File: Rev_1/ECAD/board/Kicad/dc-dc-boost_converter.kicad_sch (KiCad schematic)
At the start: 56 parts, among them Q1 IPP029N15NM6, Q2 NPN, U1 LM3478MA, U2 LM358, U3 LM358

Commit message: Components for 15V regulator are placed
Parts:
- removed C12: 1u, Capacitor_SMD:C_0805_2012Metric_Pad1.18x1.45mm_HandSolder, symbol Device:C_Small
- removed Q?: PMOS, symbol Simulation_SPICE:PMOS
- removed R? (x2): ?, symbol Device:R
- removed R?: 20m, symbol Device:R
- removed R? (x3): 10k, symbol Device:R
- added C1, C115: 100n, Capacitor_SMD:C_0603_1608Metric_Pad1.08x0.95mm_HandSolder, symbol Device:C
- added C116: 10p, Capacitor_SMD:C_0603_1608Metric_Pad1.08x0.95mm_HandSolder, symbol Device:C
- added C117, C124, C3, C4: 100n, Capacitor_SMD:C_0603_1608Metric_Pad1.08x0.95mm_HandSolder, symbol Device:C_Small
- added C118: 100u, Capacitor_SMD:CP_Elec_10x10.5, symbol Device:C_Small
- added C119: 1u, Capacitor_SMD:C_0603_1608Metric_Pad1.08x0.95mm_HandSolder, symbol Device:C_Small
- added C120: 10u, Capacitor_SMD:C_0805_2012Metric_Pad1.18x1.45mm_HandSolder, symbol Device:C_Small
- added C121: 220u, Capacitor_SMD:CP_Elec_10x10.5, symbol Device:C_Small
- added C123: 1u, Capacitor_SMD:C_0805_2012Metric_Pad1.18x1.45mm_HandSolder, symbol Device:C_Small
- added D100: D_TVS, Diode_SMD:D_0805_2012Metric_Pad1.15x1.40mm_HandSolder, symbol Device:D_TVS
- added FB100: 100, Inductor_SMD:L_0805_2012Metric_Pad1.15x1.40mm_HandSolder, symbol Device:FerriteBead_Small
- added Q101, Q2: NPN, Package_TO_SOT_SMD:SOT-23_Handsoldering, symbol Simulation_SPICE:NPN
- added Q103: PMOS, Package_TO_SOT_SMD:TO-252-2, symbol Simulation_SPICE:PMOS
- added R1, R107, R110, R14, R15, R3, R9: 10k, Resistor_SMD:R_0805_2012Metric_Pad1.20x1.40mm_HandSolder, symbol Device:R
- added R10, R11, R13, R4, R5, R8: 1k, Resistor_SMD:R_0805_2012Metric_Pad1.20x1.40mm_HandSolder, symbol Device:R
- added R109: 20m, Resistor_SMD:R_1206_3216Metric_Pad1.30x1.75mm_HandSolder, symbol Device:R
- added R111: 100k, Resistor_SMD:R_0805_2012Metric_Pad1.20x1.40mm_HandSolder, symbol Device:R
- added R112, R115, R116: 100, Resistor_SMD:R_0805_2012Metric_Pad1.20x1.40mm_HandSolder, symbol Device:R
- added R113, R114: ?, Resistor_SMD:R_0603_1608Metric_Pad0.98x0.95mm_HandSolder, symbol Device:R
- added R2: 4k7, Resistor_SMD:R_0805_2012Metric_Pad1.20x1.40mm_HandSolder, symbol Device:R
- added RV100: 10k, filip:Potentiometer_SMD_Trimmer_PVG3_3.6x3, symbol Device:R_Potentiometer_Trim
- added SW1: SW_DIP_x04, symbol Switch:SW_DIP_x04
- added unit 3 of U2
- added unit 3 of U3
- C103: renamed from C4; footprint Capacitor_SMD:C_0805_2012Metric_Pad1.18x1.45mm_HandSolder -> Capacitor_SMD:C_0603_1608Metric_Pad1.08x0.95mm_HandSolder
- C104: renamed from C5; footprint Capacitor_SMD:C_0805_2012Metric_Pad1.18x1.45mm_HandSolder -> Capacitor_SMD:C_0603_1608Metric_Pad1.08x0.95mm_HandSolder
- C105: renamed from C6; footprint Capacitor_SMD:C_0805_2012Metric_Pad1.18x1.45mm_HandSolder -> Capacitor_SMD:C_0603_1608Metric_Pad1.08x0.95mm_HandSolder
- C106: renamed from C7; footprint Capacitor_SMD:C_0805_2012Metric_Pad1.18x1.45mm_HandSolder -> Capacitor_SMD:C_0603_1608Metric_Pad1.08x0.95mm_HandSolder
- C107: renamed from C8; footprint Capacitor_SMD:C_0805_2012Metric_Pad1.18x1.45mm_HandSolder -> Capacitor_SMD:C_0603_1608Metric_Pad1.08x0.95mm_HandSolder
- C108: renamed from C9; footprint Capacitor_SMD:C_0805_2012Metric_Pad1.18x1.45mm_HandSolder -> Capacitor_SMD:C_0603_1608Metric_Pad1.08x0.95mm_HandSolder
- C109: renamed from C10; footprint Capacitor_SMD:C_0805_2012Metric_Pad1.18x1.45mm_HandSolder -> Capacitor_SMD:C_0603_1608Metric_Pad1.08x0.95mm_HandSolder
- C111: renamed from C11; footprint Capacitor_SMD:C_0805_2012Metric_Pad1.18x1.45mm_HandSolder -> Capacitor_SMD:C_0603_1608Metric_Pad1.08x0.95mm_HandSolder
- C2: renamed from C?; footprint (none) -> Capacitor_SMD:C_0603_1608Metric_Pad1.08x0.95mm_HandSolder
- D1, D2: renamed from D?; footprint (none) -> LED_SMD:LED_0805_2012Metric_Pad1.15x1.40mm_HandSolder
- L100: renamed from L1; footprint filip:IHLP5050FD -> filip:L_IHLP5050FD_5.0x5.0mm_Shielded
- Q1: renamed from Q?; footprint (none) -> Package_TO_SOT_SMD:SOT-23_Handsoldering; Mouser NO: (none) -> 637-BC817-16
- Q100: renamed from Q1; footprint filip:PSMN4R0 -> filip:TO-263-5_TabPin1-HandSoldered
- Q102: renamed from Q2; footprint (none) -> Package_TO_SOT_SMD:SOT-223-3_TabPin2; Mouser NO: (none) -> 621-ZXTN19100CGTA
- R100: renamed from R1; footprint Resistor_SMD:R_0805_2012Metric_Pad1.20x1.40mm_HandSolder -> Resistor_SMD:R_0603_1608Metric_Pad0.98x0.95mm_HandSolder
- R104: renamed from R5; footprint Resistor_SMD:R_0805_2012Metric_Pad1.20x1.40mm_HandSolder -> Resistor_SMD:R_0603_1608Metric_Pad0.98x0.95mm_HandSolder
- R106, R108, R17, R18, R19, R20, R21, R6, R7: renamed from R?; footprint (none) -> Resistor_SMD:R_0805_2012Metric_Pad1.20x1.40mm_HandSolder
- R12, R16: renamed from R?; footprint (none) -> Resistor_SMD:R_0603_1608Metric_Pad0.98x0.95mm_HandSolder
- R22, R23: renamed from R?; value 5k1 -> 4k7; footprint (none) -> Resistor_SMD:R_0805_2012Metric_Pad1.20x1.40mm_HandSolder
- R24: renamed from R?; value 10k -> 1K; footprint (none) -> Resistor_SMD:R_0805_2012Metric_Pad1.20x1.40mm_HandSolder
- gave numbers to parts that had none: 2
- renumbered C1 to C100, C2 to C101, C3 to C102, C13 to C112, C14 to C113, C15 to C114, D1 to D101, D2 to D102, R2 to R101, R3 to R102, R4 to R103, R6 to R105, U1 to U100
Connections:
- net +17V: now also Q102.2 (C), C115.2, C123.1, FB100.2, Q101.1 (C), R107.1, U2.8 (V+); no longer C111.1, C112.1, C113.1, C114.1, D101.2 (K), Q102.1 (C), R103.1
- net +5V: now also C1.2, C3.1, C4.1, R1.1, U3.8 (V+)
- net CURRENT_V_REF: now also R10.2, R11.2, R13.2, R15.2, R5.2
- net GND: now also C1.1, C115.1, C117.2, C118.2, C119.2, C120.2, C121.2, C123.2, C124.2, C3.2, C4.2, D100.1 (A1), Q2.3 (E), R111.2, R114.2, U2.4 (V-), U3.4 (V-)
- net RESET: now also C2.2
- net SHUNT_IN: now also C117.1, C118.1, R109.1
- net SHUNT_OUT: now also Q103.3 (S), R109.2, R110.1
- net SHUTDOWN: now also R112.2, R115.1
- net V_FB: now also C116.2, R113.2, R114.1
- net V_REF: now also C124.1, R107.2
- net at R108.1, U2.1: now also C116.1
- net at R108.2: now also Q101.2 (B); no longer Q102.2 (B)
- net VIN renamed V_IN
- net V_IN: now also D100.2 (A2)
- new net: Q2.2 (B), R115.2
- new net: R1.2, SW1.1, SW1.2, SW1.3, SW1.4
- new net: Q2.1 (C), R116.1
- new net: R10.1, R11.1, R4.2
- new net: R13.1, R8.2
- new net: R5.1, SW1.8
- new net: Q101.3 (E), Q102.1 (B)
- new net: R14.2, R15.1
- new net: R113.1, RV100.2
- new net: R4.1, SW1.7
- new net: R14.1, R9.2
- new net: R3.2, R9.1
- new net: R3.1, SW1.5
- new net: R2.1, SW1.6
- new net: R2.2, R8.1
- new net +15V: C119.1, C120.1, C121.1, Q103.2 (D), R116.2, RV100.1
- new net LOOP_OUT: C111.1, C112.1, C113.1, C114.1, D101.2 (K), FB100.1, R103.1
- new net MOS_G: Q103.1 (G), R110.2, R111.1, R112.1
- no-connect marks 0 -> 1
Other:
- note added: "0.5A"
- note added: "15V DC-DC"
- note added: "1A"
- note added: "2A"
- note added: "4A"
- note added: ">=100mA"
- note added: ">=5-6A"
- note added: "Bypass & Bulk Caps"
- note added: "LOW RDS_ON"
- note added: "Only 1 DIP-Switch can be used at once!"
- note added: "TODO: Fel voltage divider Sätt ut GND och lös hur det ska koppls till current_V_REF"
- note added: "Vout = 1.26(1+((R103+R104)/R105))"
- moved on the sheet: C100, C101, C102, C103, C104, C105, C106, C107, C108, C109, C111, C112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

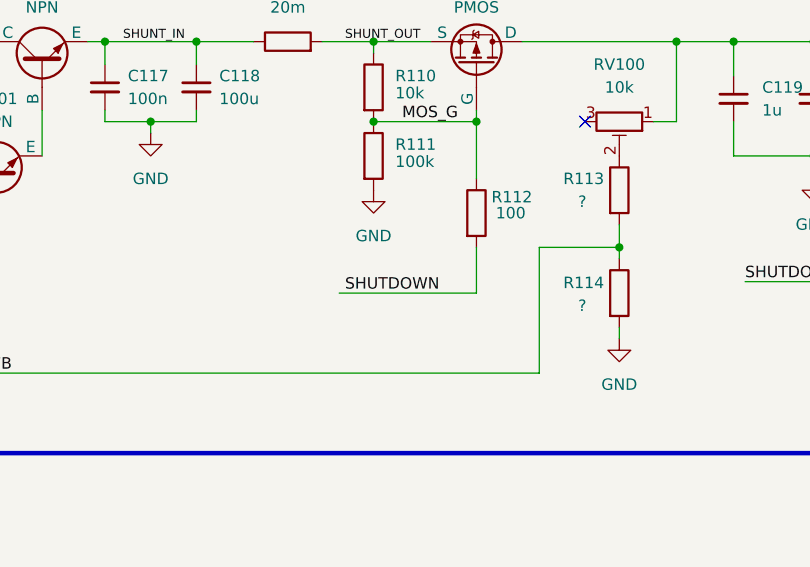
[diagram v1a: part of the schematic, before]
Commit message: Moved Input Capacitors to minimize loop area and created pours for boost converter
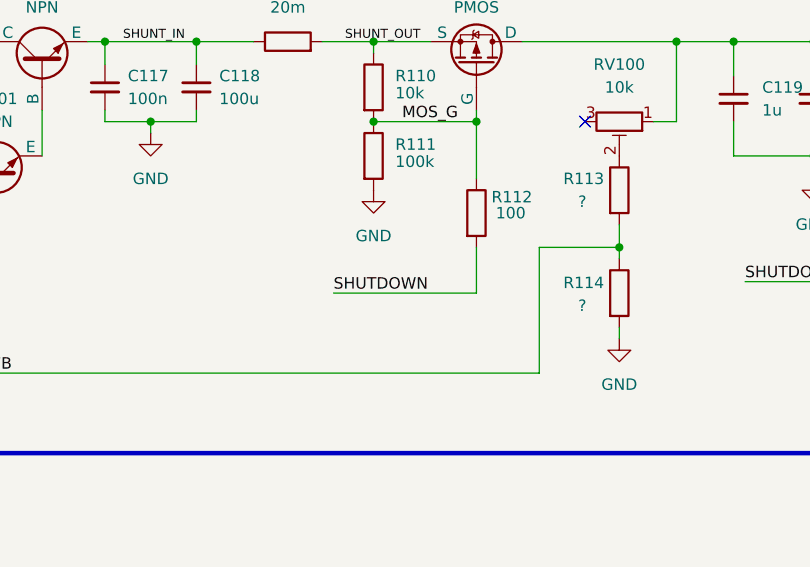
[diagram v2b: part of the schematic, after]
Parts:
- Q100: footprint filip:TO-263-5_TabPin1-HandSoldered -> filip:TO-263-4_TabPin1-HandSoldered
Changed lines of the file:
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@@
 	(wire
 		(pts
+			(xy 298.45 91.44) (xy 314.325 91.44)
+		)
+		(stroke
+			(width 0)
+			(type default)
+		)
+	)
+	(wire
+		(pts
 			(xy 106.68 80.01) (xy 100.33 80.01)
 		)
@@
 	(wire
 		(pts
-			(xy 314.325 91.44) (xy 299.085 91.44)
-		)
-		(stroke
-			(width 0)
-			(type default)
-		)
-	)
-	(wire
-		(pts
 			(xy 110.49 186.69) (xy 103.505 186.69)
 		)
@@
 	)
 	(label "SHUTDOWN"
-		(at 299.72 91.44 0)
-		(effects
-			(font
-				(size 1.27 1.27)
-			)
-			(justify left bottom)
-		)
-	)
-	(label "SHUTDOWN"
 		(at 269.24 185.42 180)
 		(effects
@@
 		)
 	)
+	(label "SHUTDOWN"
+		(at 298.45 91.44 0)
+		(effects
+			(font
+				(size 1.27 1.27)
+			)
+			(justify left bottom)
+		)
+	)
 	(label "FA{slash}SD"
 		(at 61.595 85.09 0)
@@
 			)
 		)
-		(property "Footprint" "filip:TO-263-5_TabPin1-HandSoldered"
+		(property "Footprint" "filip:TO-263-4_TabPin1-HandSoldered"
 			(at 120.65 72.39 0)
 			(effects

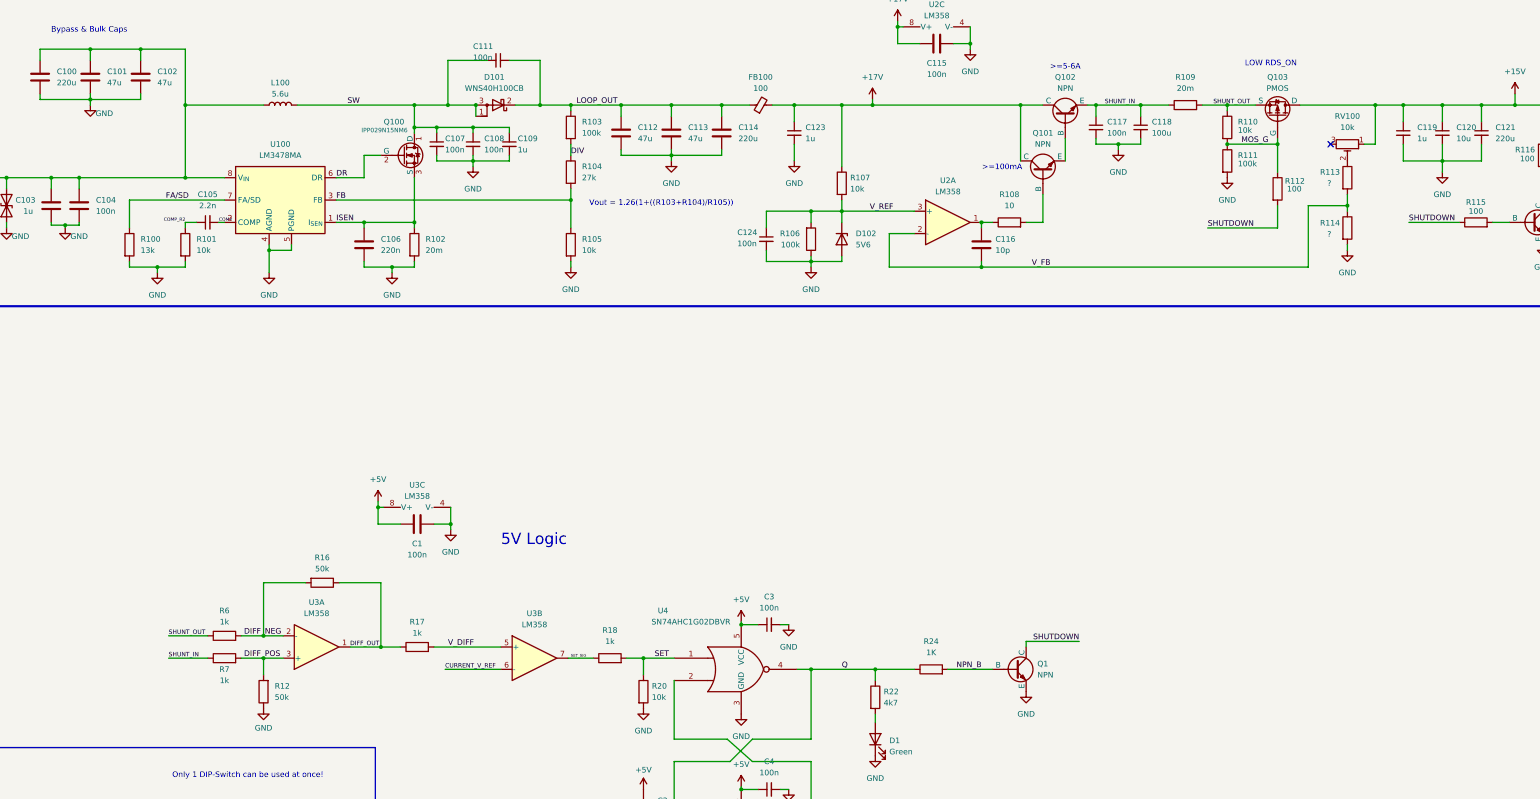
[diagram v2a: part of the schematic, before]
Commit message: Added inverted buck-boost for -17V rail
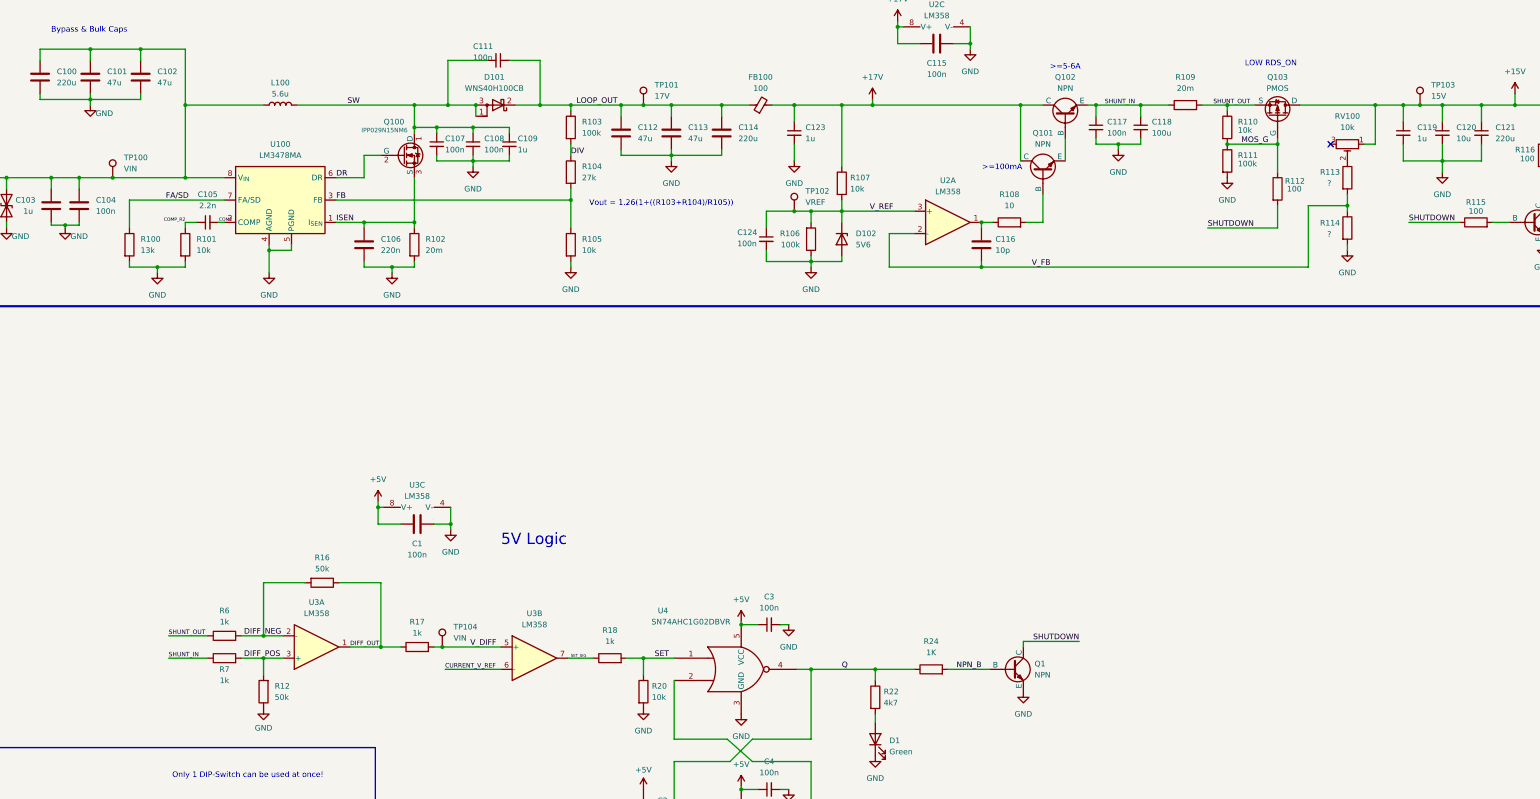
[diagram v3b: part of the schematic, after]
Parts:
- added TP100, TP104: VIN, Connector_Pin:Pin_D0.7mm_L6.5mm_W1.8mm_FlatFork, symbol Connector:TestPoint
- added TP101: 17V, Connector_Pin:Pin_D0.7mm_L6.5mm_W1.8mm_FlatFork, symbol Connector:TestPoint
- added TP102: VREF, Connector_Pin:Pin_D0.7mm_L6.5mm_W1.8mm_FlatFork, symbol Connector:TestPoint
- added TP103: 15V, Connector_Pin:Pin_D0.7mm_L6.5mm_W1.8mm_FlatFork, symbol Connector:TestPoint
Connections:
- net +15V: now also TP103.1
- net LOOP_OUT: now also TP101.1
- net V_DIFF: now also TP104.1
- net V_IN: now also TP100.1
- net V_REF: now also TP102.1
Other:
- moved on the sheet: Q1

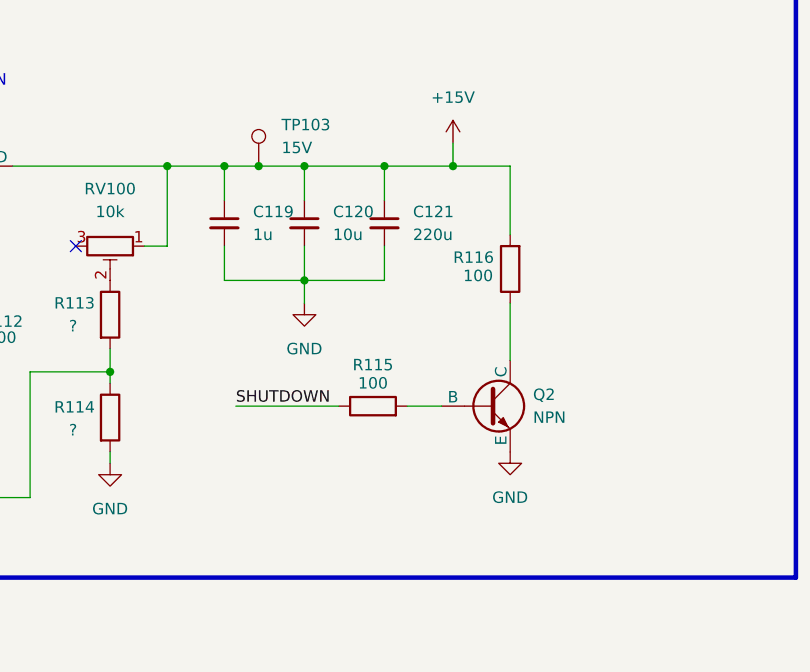
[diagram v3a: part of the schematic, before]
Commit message: Added Heatsink to Transistors
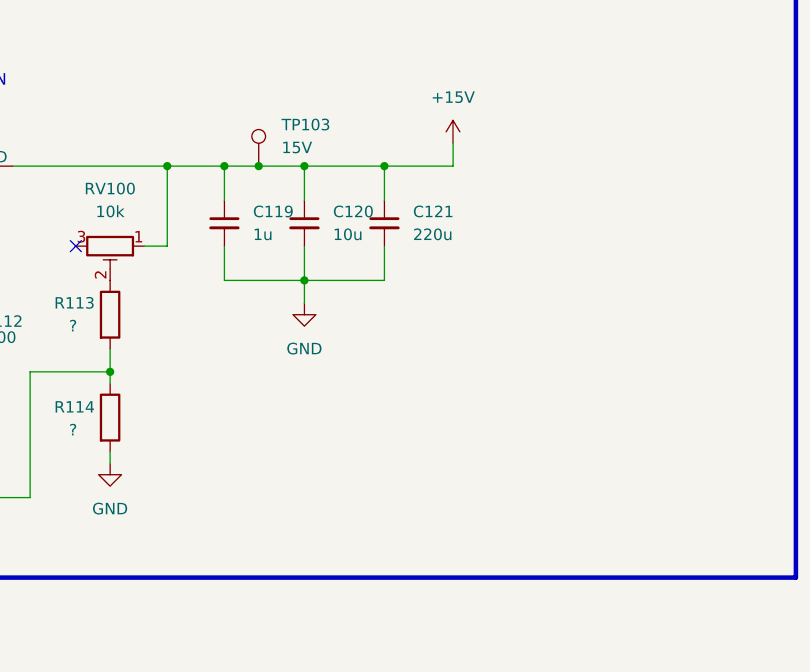
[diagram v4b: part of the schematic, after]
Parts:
- removed Q2: NPN, Package_TO_SOT_SMD:SOT-23_Handsoldering, symbol Simulation_SPICE:NPN
- removed R115, R116: 100, Resistor_SMD:R_0805_2012Metric_Pad1.20x1.40mm_HandSolder, symbol Device:R
- D101: footprint Package_TO_SOT_THT:TO-220-3_Vertical -> filip:TO-220-3 with HeatSink
- Q102: footprint Package_TO_SOT_SMD:SOT-223-3_TabPin2 -> filip:TO-220-3 with HeatSink
